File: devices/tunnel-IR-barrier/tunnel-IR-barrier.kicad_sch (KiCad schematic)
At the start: 20 parts, among them J1 JST SH, J2 JST SH, J4 JST SH, Q1 Q_NMOS_GSD, Q2 Q_NMOS_GSD, Q3 Q_NMOS_GSD, U1 GP2S700HCP, U2 ATtiny204-SS, U3 GP2S700HCP, U4 GP2S700HCP

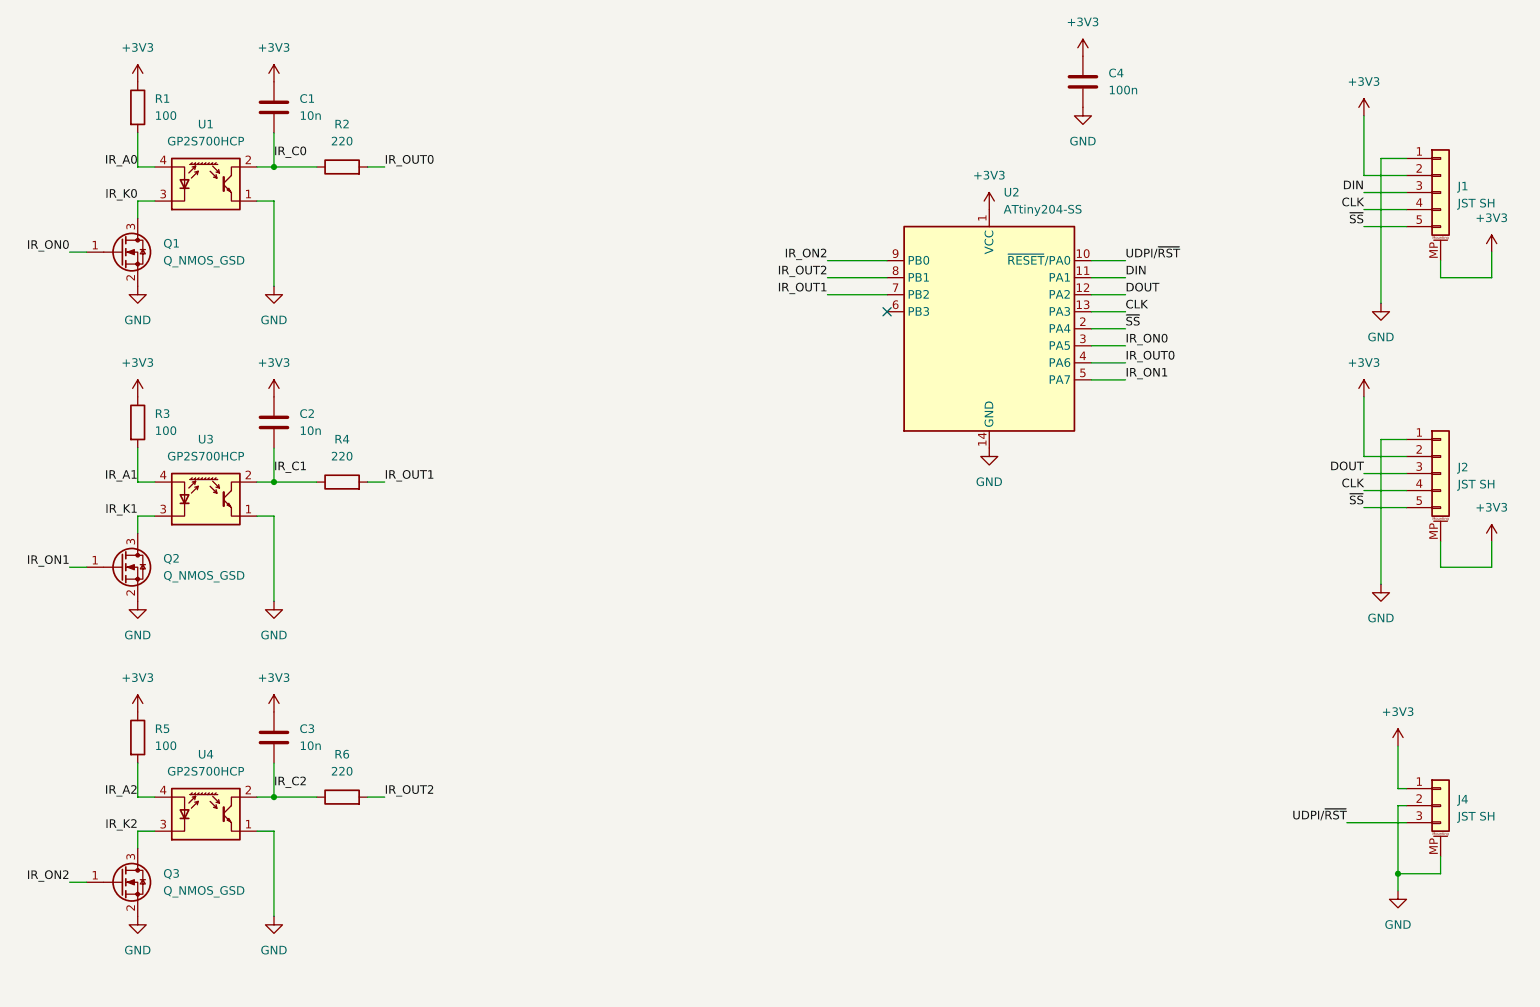
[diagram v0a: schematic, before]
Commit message: Update IR barrier for easier firmware implementation
Uses a common readout circuitry, and a high-side switch to not have to switch pin direction with interupts
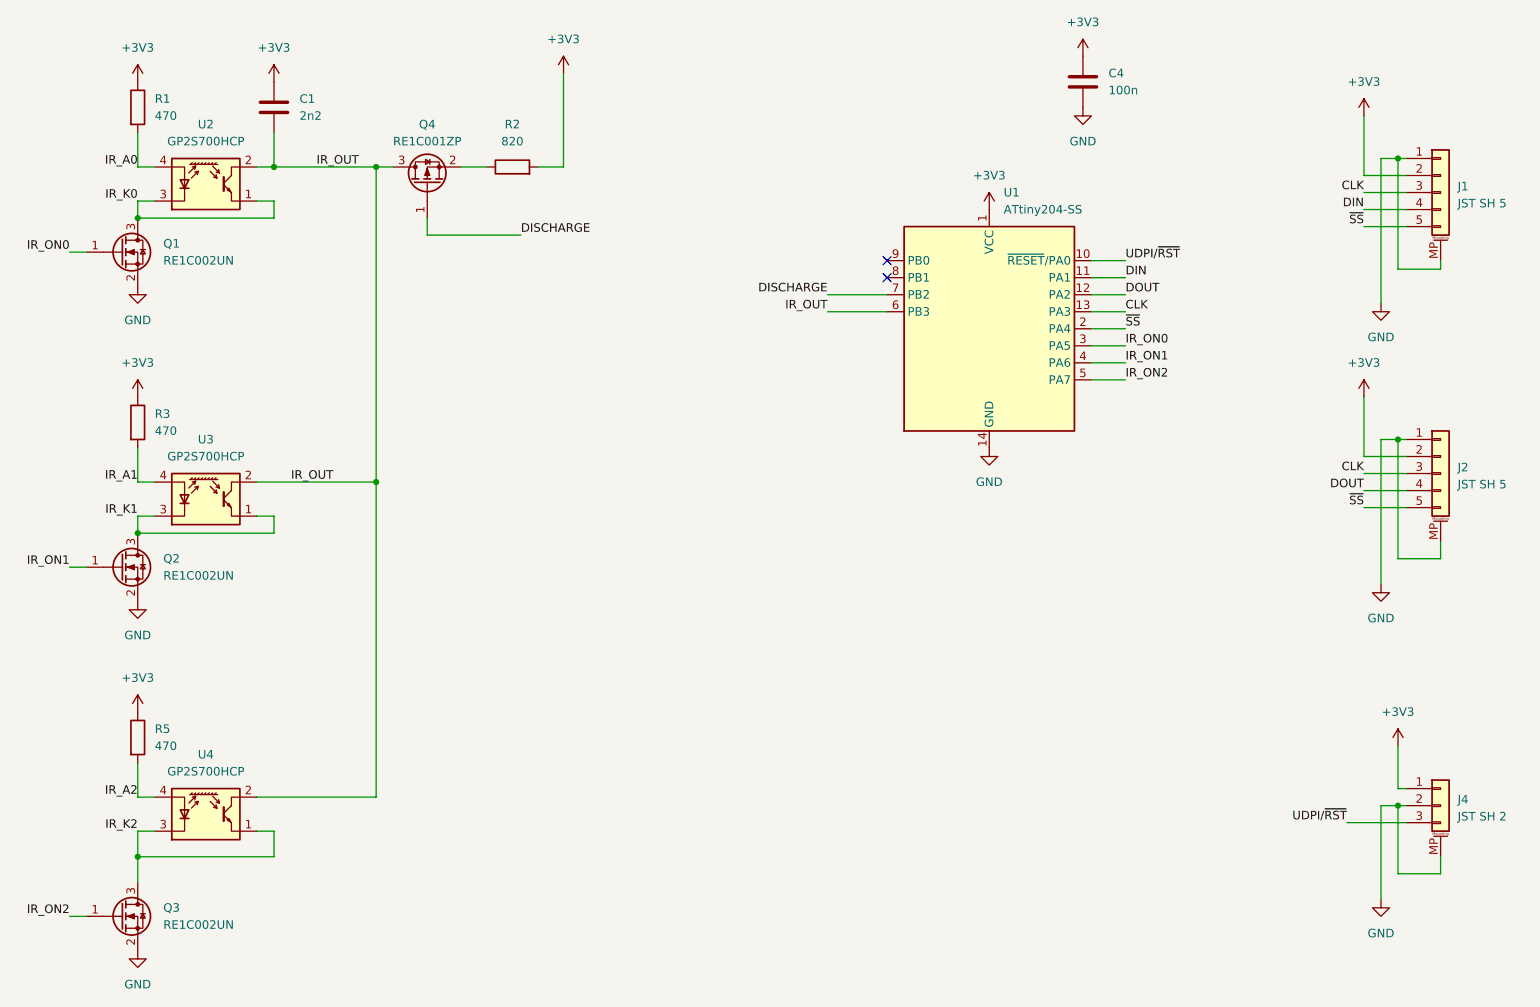
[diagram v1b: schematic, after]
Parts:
- removed C2, C3: 10n, Capacitor_SMD:C_0402_1005Metric, symbol Device:C
- removed R4, R6: 220, Resistor_SMD:R_0402_1005Metric, symbol Device:R
- added Q4: RE1C001ZP, Package_TO_SOT_SMD:SOT-416, symbol Transistor_FET:Q_PMOS_GSD
- C1: value 10n -> 2n2; footprint Capacitor_SMD:C_0402_1005Metric -> Capacitor_SMD:C_0603_1608Metric; MPN GRM155R71C103KA01D -> GRM1885C1H222JA01D
- C4: footprint Capacitor_SMD:C_0402_1005Metric -> Capacitor_SMD:C_0603_1608Metric; MPN CL05B104KP5NNNC -> CL10B104KB8NNWC
- J1, J2: value JST SH -> JST SH 5; footprint Connector_JST:JST_SH_SM05B-SRSS-TB_1x05-1MP_P1.00mm_Horizontal -> Connector_JST:JST_SH_BM05B-SRSS-TB_1x05-1MP_P1.00mm_Vertical
- J4: value JST SH -> JST SH 2; footprint Connector_JST:JST_SH_SM03B-SRSS-TB_1x03-1MP_P1.00mm_Horizontal -> Connector_JST:JST_SH_BM03B-SRSS-TB_1x03-1MP_P1.00mm_Vertical
- Q1, Q2, Q3: value Q_NMOS_GSD -> RE1C002UN
- R1, R3, R5: value 100 -> 470; footprint Resistor_SMD:R_0402_1005Metric -> Resistor_SMD:R_0603_1608Metric; MPN RC0402FR-07100RL -> RC0603FR-07470RL
- R2: value 220 -> 820; footprint Resistor_SMD:R_0402_1005Metric -> Resistor_SMD:R_0603_1608Metric; MPN RC0402FR-07220RL -> RC0603FR-07820RL
- renumbered U2 to U1, U1 to U2
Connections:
- net IR_C1 is gone; now on net IR_OUT: U3.2
- net IR_C2 is gone; now on net IR_OUT: U4.2
- net +3V3: now also R2.2; no longer J1.MP (MountPin), J2.MP (MountPin)
- net CLK: now also J1.3 (Pin_3), J2.3 (Pin_3); no longer J1.4 (Pin_4), J2.4 (Pin_4)
- net DIN: now also J1.4 (Pin_4); no longer J1.3 (Pin_3)
- net DOUT: now also J2.4 (Pin_4); no longer J2.3 (Pin_3)
- net GND: now also J1.MP (MountPin), J2.MP (MountPin); no longer U2.1, U3.1, U4.1
- net IR_K0: now also U2.1
- net IR_K1: now also U3.1
- net IR_K2: now also U4.1
- net IR_ON1: now also U1.4 (PA6); no longer U1.5 (PA7)
- net IR_ON2: now also U1.5 (PA7); no longer U1.9 (PB0)
- net IR_OUT: now reaches U1.6 (PB3)
- net IR_OUT: now also C1.2, U2.2, Q4.3 (D)
- removed net IR_C0: C1.2, R2.1, U2.2
- removed net IR_OUT0: R2.2, U1.4 (PA6)
- net IR_OUT1 renamed DISCHARGE
- net DISCHARGE: now also Q4.1 (G)
- net IR_OUT2: no longer names the net of U1.8 (PB1)
- new net: Q4.2 (S), R2.1
- no-connect marks 1 -> 2
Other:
- moved on the sheet: Q3, R2
